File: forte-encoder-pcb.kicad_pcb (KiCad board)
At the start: 6 copper layers, 36.5 x 45 mm, 54 parts, among them J1 Conn_01x01_Pin, J10 Conn_01x01_Pin, J2 BM07B-GHS-TBT, J4 Conn_01x01_Pin, J7 Conn_01x01_Pin, J8 Conn_01x01_Pin, J9 Conn_01x01_Pin, U2 STM32F103C8Tx, U3 MCP2542FD-E/MF, U4 MA732GQ-Z, U5 TPS629203DRLR, U6 TPS629203DRLR, Y1 CSTNE8M00G550000R0

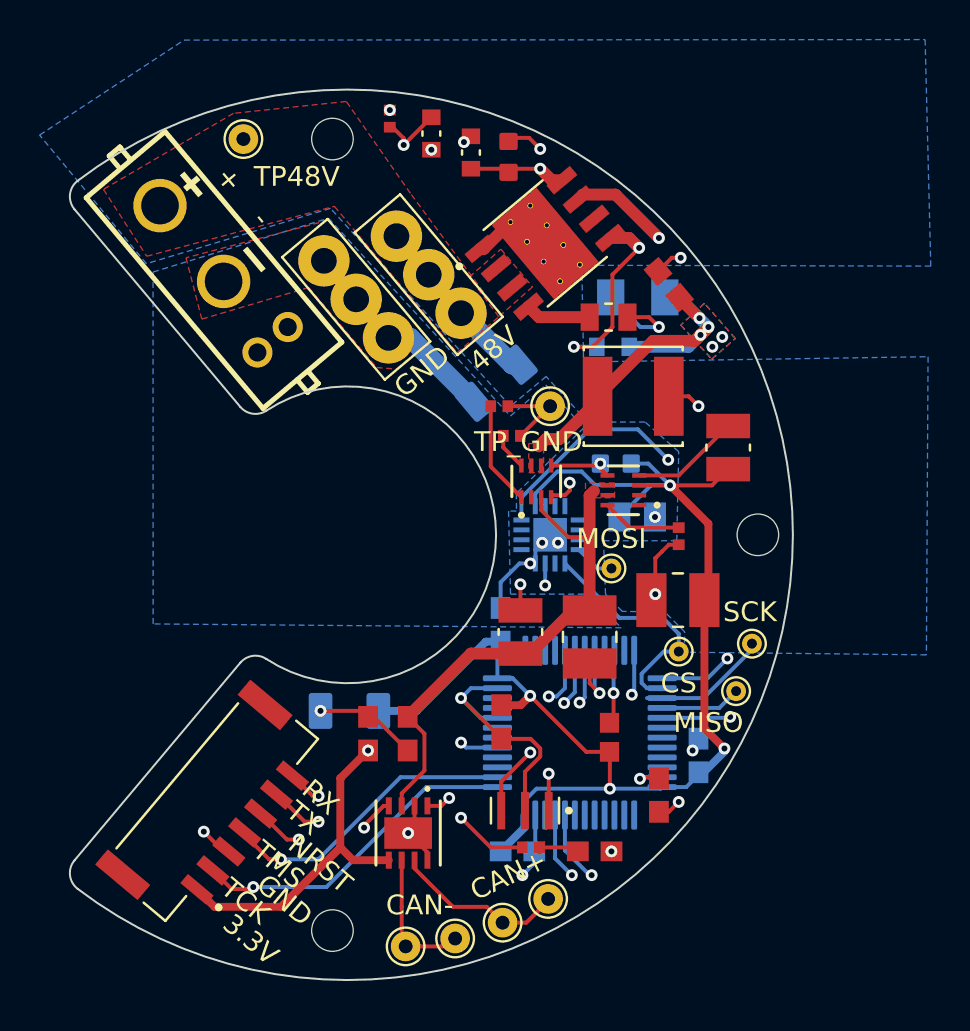
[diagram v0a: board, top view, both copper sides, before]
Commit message: fix TMS PA15->PA13
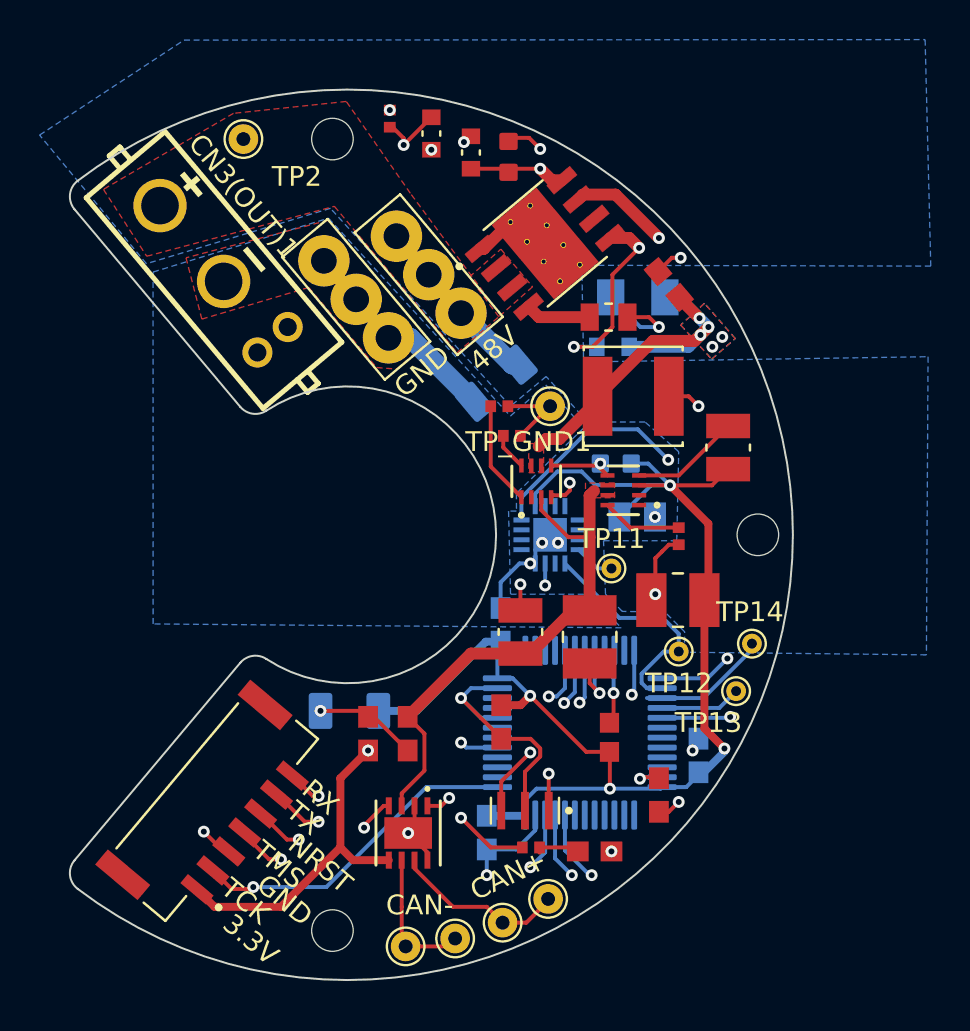
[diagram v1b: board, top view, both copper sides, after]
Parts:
- CN3(OUT)1: renamed from +    -
- moved C29 1.82 mm to (102.8, 115.0), turned to 90 degrees
- renumbered MOSI to TP11, CS to TP12, MISO to TP13, SCK to TP14, TP48V to TP2, TP_GND to TP_GND1
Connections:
- U2 pad 34: unconnected-(U2-PA13-Pad34) -> /TMS
- U2 pad 38: /TMS -> unconnected-(U2-PA15-Pad38)
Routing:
- net /TMS: track 15.1 -> 18.2 mm, vias 1 -> 2
- net GND: track 62.7 -> 64.7 mm
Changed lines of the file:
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@@
 		(layer "F.Cu")
 		(at 89.130397 86.75304 -50)
-		(property "Reference" "+    -"
+		(property "Reference" "CN3(OUT)1"
 			(at -2.071236 -3.525863 130)
 			(layer "F.SilkS")
@@
 		(descr "THT pad as test Point, diameter 1.0mm, hole diameter 0.5mm")
 		(tags "test point THT pad")
-		(property "Reference" "MOSI"
+		(property "Reference" "TP11"
 			(at 0 1.5 0)
 			(layer "F.SilkS")
@@
 		(descr "THT pad as test Point, diameter 1.0mm, hole diameter 0.5mm")
 		(tags "test point THT pad")
-		(property "Reference" "MISO"
+		(property "Reference" "TP13"
 			(at 1.4 -1.6 0)
 			(layer "F.SilkS")
@@
 		(descr "THT pad as test Point, diameter 1.0mm, hole diameter 0.5mm")
 		(tags "test point THT pad")
-		(property "Reference" "SCK"
+		(property "Reference" "TP14"
 			(at 0.1 1.6 0)
 			(layer "F.SilkS")
@@
 		(descr "THT pad as test Point, diameter 1.5mm, hole diameter 0.7mm")
 		(tags "test point THT pad")
-		(property "Reference" "TP_GND"
+		(property "Reference" "TP_GND1"
 			(at 1.1 -1.8 0)
 			(layer "F.SilkS")
@@
 		(descr "THT pad as test Point, diameter 1.5mm, hole diameter 0.7mm")
 		(tags "test point THT pad")
-		(property "Reference" "TP48V"
+		(property "Reference" "TP2"
 			(at 2.7 1.9 0)
 			(layer "F.SilkS")
@@
 		(descr "THT pad as test Point, diameter 1.0mm, hole diameter 0.5mm")
 		(tags "test point THT pad")
-		(property "Reference" "CS"
+		(property "Reference" "TP12"
 			(at 0 -1.6 0)
 			(layer "F.SilkS")
@@
 			(layers "B.Cu" "B.Mask" "B.Paste")
 			(roundrect_rratio 0.25)
-			(net "unconnected-(U2-PA13-Pad34)")
+			(net "/TMS")
 			(pinfunction "PA13_34")
-			(pintype "bidirectional+no_connect")
+			(pintype "bidirectional")
 		)
 		(pad "35" smd roundrect
@@
 			(layers "B.Cu" "B.Mask" "B.Paste")
 			(roundrect_rratio 0.25)
-			(net "/TMS")
+			(net "unconnected-(U2-PA15-Pad38)")
 			(pinfunction "PA15_38")
-			(pintype "bidirectional")
+			(pintype "bidirectional+no_connect")
 		)
 		(pad "39" smd roundrect
@@
 	(footprint "dash:CC0603JRX7R9BB104"
 		(layer "B.Cu")
-		(at 104.35 116 180)
+		(at 102.8 115.05 90)
 		(descr "<b>CAPACITOR</b>")
 		(property "Reference" "C29"
-			(at -0.235808 1.239253 0)
+			(at -0.235808 1.239253 90)
 			(layer "B.SilkS")
 			(hide yes)
@@
 		)
 		(property "Value" "100nF 50V"
-			(at 1.567319 -1.206787 0)
+			(at 1.567319 -1.206787 90)
 			(layer "B.Fab")
 			(effects
@@
 		)
 		(property "Datasheet" ""
-			(at 0 0 0)
+			(at 0 0 90)
 			(layer "B.Fab")
 			(hide yes)
@@
 		)
 		(property "Description" ""
-			(at 0 0 0)
+			(at 0 0 90)
 			(layer "B.Fab")
 			(hide yes)
@@
 		(duplicate_pad_numbers_are_jumpers no)
 		(fp_line
-			(start 1.673 0.783)
-			(end 1.673 -0.783)
+			(start 1.673 -0.783)
+			(end -1.673 -0.783)
 			(stroke
 				(width 0.0508)
@@
 		)
 		(fp_line
-			(start 1.673 -0.783)
-			(end -1.673 -0.783)
+			(start -1.673 -0.783)
+			(end -1.673 0.783)
 			(stroke
 				(width 0.0508)
@@
 		)
 		(fp_line
-			(start -1.673 0.783)
-			(end 1.673 0.783)
+			(start 1.673 0.783)
+			(end 1.673 -0.783)
 			(stroke
 				(width 0.0508)
@@
 		)
 		(fp_line
-			(start -1.673 -0.783)
-			(end -1.673 0.783)
+			(start -1.673 0.783)
+			(end 1.673 0.783)
 			(stroke
 				(width 0.0508)
@@
 		)
 		(fp_line
-			(start -0.356 0.432)
-			(end 0.356 0.432)
+			(start -0.356 -0.419)
+			(end 0.356 -0.419)
 			(stroke
 				(width 0.1016)
@@
 		)
 		(fp_line
-			(start -0.356 -0.419)
-			(end 0.356 -0.419)
+			(start -0.356 0.432)
+			(end 0.356 0.432)
 			(stroke
 				(width 0.1016)
@@
 		)
 		(pad "1" smd rect
-			(at -0.85 0 180)
+			(at -0.85 0 90)
 			(size 1.1 1)
 			(layers "B.Cu" "B.Mask" "B.Paste")
@@
 		)
 		(pad "2" smd rect
-			(at 0.85 0 180)
+			(at 0.85 0 90)
 			(size 1.1 1)
 			(layers "B.Cu" "B.Mask" "B.Paste")
@@
 	)
 	(segment
-		(start 103.5 116)
-		(end 104.7 114.8)
+		(start 104.6625 114.2)
+		(end 104.7 114.1625)
 		(width 0.4)
 		(layer "B.Cu")
@@
 	)
 	(segment
-		(start 105.314449 112.828141)
-		(end 109.02 112.828141)
-		(width 0.2)
+		(start 102.8 114.2)
+		(end 104.6625 114.2)
+		(width 0.4)
 		(layer "B.Cu")
 		(net "+3.3V")
 	)
 	(segment
-		(start 104.7 114.8)
-		(end 104.7 114.1625)
-		(width 0.4)
+		(start 105.314449 112.828141)
+		(end 109.02 112.828141)
+		(width 0.2)
 		(layer "B.Cu")
 		(net "+3.3V")
@@
 	)
 	(via
-		(at 104.6 117.2)
+		(at 102.8 117.2)
 		(size 0.6)
 		(drill 0.3)
@@
 	)
 	(segment
+		(start 102.8 115.9)
+		(end 102.8 117.2)
+		(width 0.2)
+		(layer "B.Cu")
+		(net "GND")
+	)
+	(segment
 		(start 109.062 88)
 		(end 110.562 89.5)
@@
 	)
 	(segment
+		(start 102.8 115.9)
+		(end 104.28241 115.9)
+		(width 0.2)
+		(layer "B.Cu")
+		(net "GND")
+	)
+	(segment
+		(start 105.25 114.93241)
+		(end 105.25 114.1625)
+		(width 0.2)
+		(layer "B.Cu")
+		(net "GND")
+	)
+	(segment
 		(start 101.5 108.25)
 		(end 102.5 109.25)
@@
 	)
 	(segment
-		(start 105.2 116.6)
-		(end 104.6 117.2)
-		(width 0.2)
-		(layer "B.Cu")
-		(net "GND")
-	)
-	(segment
 		(start 104.4522 101.4478)
 		(end 105 101.4478)
@@
 	)
 	(segment
-		(start 105.2 116)
-		(end 105.2 116.6)
-		(width 0.2)
-		(layer "B.Cu")
-		(net "GND")
-	)
-	(segment
 		(start 110.562 89.5)
 		(end 111.5 89.5)
@@
 	)
 	(segment
-		(start 105.25 114.1625)
-		(end 105.25 115.61)
+		(start 105.6 100.4)
+		(end 106 100)
 		(width 0.2)
 		(layer "B.Cu")
@@
 	)
 	(segment
-		(start 105.6 100.4)
-		(end 106 100)
+		(start 104.28241 115.9)
+		(end 105.25 114.93241)
 		(width 0.2)
 		(layer "B.Cu")
@@
 	)
 	(via
+		(at 105 116.8)
+		(size 0.6)
+		(drill 0.3)
+		(layers "F.Cu" "B.Cu")
+		(net "/TMS")
+	)
+	(via
 		(at 92.4 116.4)
 		(size 0.6)
@@
 	)
 	(segment
-		(start 98.442893 112.25)
-		(end 103.3375 112.25)
+		(start 105.75 116.05)
+		(end 105 116.8)
 		(width 0.2)
 		(layer "B.Cu")
@@
 	)
 	(segment
-		(start 94.292893 116.4)
-		(end 98.442893 112.25)
+		(start 105.75 114.1625)
+		(end 105.75 116.05)
 		(width 0.2)
 		(layer "B.Cu")
@@
 	)
 	(segment
+		(start 104.6 116.4)
+		(end 105 116.8)
+		(width 0.2)
+		(layer "In3.Cu")
+		(net "/TMS")
+	)
+	(segment
 		(start 92.4 116.4)
-		(end 94.292893 116.4)
+		(end 104.6 116.4)
 		(width 0.2)
-		(layer "B.Cu")
+		(layer "In3.Cu")
 		(net "/TMS")
 	)

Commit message: swap can
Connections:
- CN3(OUT)1 pad 1: /CAN+ -> /CAN-
- CN3(OUT)1 pad 2: /CAN- -> /CAN+
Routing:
- net /CAN+: track 49.8 -> 50.7 mm
- net /CAN-: track 49.4 -> 48.6 mm
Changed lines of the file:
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@@
 			(layers "*.Cu" "*.Mask")
 			(remove_unused_layers no)
-			(net "/CAN+")
+			(net "/CAN-")
 			(pintype "unspecified")
 			(thermal_bridge_angle 90)
@@
 			(layers "*.Cu" "*.Mask")
 			(remove_unused_layers no)
-			(net "/CAN-")
+			(net "/CAN+")
 			(pintype "unspecified")
 			(thermal_bridge_angle 90)
@@
 	)
 	(segment
-		(start 92.323112 91.9)
-		(end 91.208687 90.785575)
+		(start 98.7 120.8)
+		(end 97.95 120.05)
 		(width 0.2)
 		(layer "In1.Cu")
@@
 	)
 	(segment
-		(start 98.7 120.8)
-		(end 97.95 120.05)
+		(start 97.8 91.9)
+		(end 95.140776 91.9)
 		(width 0.2)
 		(layer "In1.Cu")
@@
 	)
 	(segment
-		(start 99 108)
-		(end 104 103)
+		(start 100.045753 92.545753)
+		(end 98.445753 92.545753)
 		(width 0.2)
 		(layer "In1.Cu")
@@
 	)
 	(segment
-		(start 104 96.5)
-		(end 100.045753 92.545753)
+		(start 97.95 120.05)
+		(end 97.95 109.05)
 		(width 0.2)
 		(layer "In1.Cu")
@@
 	)
 	(segment
-		(start 98.445753 92.545753)
-		(end 97.8 91.9)
+		(start 104 96.5)
+		(end 100.045753 92.545753)
 		(width 0.2)
 		(layer "In1.Cu")
@@
 	)
 	(segment
-		(start 100.045753 92.545753)
-		(end 98.445753 92.545753)
+		(start 97.95 109.05)
+		(end 104 103)
 		(width 0.2)
 		(layer "In1.Cu")
@@
 	)
 	(segment
-		(start 97.95 109.05)
-		(end 99 108)
+		(start 95.140776 91.9)
+		(end 92.740776 89.5)
 		(width 0.2)
 		(layer "In1.Cu")
@@
 	)
 	(segment
-		(start 97.8 91.9)
-		(end 92.323112 91.9)
+		(start 98.445753 92.545753)
+		(end 97.8 91.9)
 		(width 0.2)
 		(layer "In1.Cu")
@@
 	)
 	(segment
-		(start 97.95 120.05)
-		(end 97.95 109.05)
+		(start 92.740776 89.740776)
+		(end 92.740776 89.5)
 		(width 0.2)
-		(layer "In1.Cu")
+		(layer "In2.Cu")
 		(net "/CAN-")
 	)
@@
 	)
 	(segment
-		(start 92.740776 89.740776)
-		(end 92.740776 89.5)
-		(width 0.2)
-		(layer "In2.Cu")
-		(net "/CAN+")
-	)
-	(segment
-		(start 99.5 115.5)
-		(end 99.5 108)
+		(start 103.6 119.6)
+		(end 99.5 115.5)
 		(width 0.2)
 		(layer "In2.Cu")
@@
 	)
 	(segment
-		(start 99.5 108)
-		(end 104 103.5)
+		(start 104 96.5)
+		(end 99.5 92)
 		(width 0.2)
 		(layer "In2.Cu")
@@
 	)
 	(segment
-		(start 95 92)
-		(end 92.740776 89.740776)
+		(start 99.5 115.5)
+		(end 99.5 108)
 		(width 0.2)
 		(layer "In2.Cu")
@@
 	)
 	(segment
-		(start 104 96.5)
-		(end 99.5 92)
+		(start 92.423112 92)
+		(end 91.208687 90.785575)
 		(width 0.2)
 		(layer "In2.Cu")
@@
 	)
 	(segment
-		(start 99.5 92)
-		(end 95 92)
+		(start 99.5 108)
+		(end 104 103.5)
 		(width 0.2)
 		(layer "In2.Cu")
@@
 	)
 	(segment
-		(start 103.6 119.6)
-		(end 99.5 115.5)
+		(start 99.5 92)
+		(end 92.423112 92)
 		(width 0.2)
 		(layer "In2.Cu")

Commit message: some shifts
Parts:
- moved TP2 4.90 mm to (95.4, 79.8)
- moved H1 3.41 mm to (91.6, 80.3)
- moved H3 3.41 mm to (91.6, 119.7)
- moved J8 3.02 mm to (96.2, 119.1)
- moved C31 2.78 mm to (106.2, 103.7), turned to 180 degrees
- moved J9 2.64 mm to (98.9, 119.1)
- moved C32 2.54 mm to (95.4, 111.4)
- moved J10 2.21 mm to (101.5, 118.9)
- moved J7 1.81 mm to (104.1, 118.2)
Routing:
- net +3.3V: track 96.5 -> 101.8 mm
- net /CAN+: track 50.7 -> 46.9 mm
- net /CAN-: track 48.6 -> 45.4 mm
- net GND: track 64.7 -> 67.3 mm

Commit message: more fix
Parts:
- removed TP_GND1: GND TestPoint, TestPoint:TestPoint_THTPad_D1.5mm_Drill0.7mm
- moved C37 1.92 mm to (105.0, 93.2), turned to 130 degrees
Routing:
- net GND: track 67.3 -> 61.6 mm, vias 17 -> 18
- net +48V: track 5.34 -> 1.36 mm
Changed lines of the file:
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@@
 		)
 	)
-	(footprint "TestPoint:TestPoint_THTPad_D1.5mm_Drill0.7mm"
-		(layer "F.Cu")
-		(at 106 93.5 180)
-		(descr "THT pad as test Point, diameter 1.5mm, hole diameter 0.7mm")
-		(tags "test point THT pad")
-		(property "Reference" "TP_GND1"
-			(at 1.1 -1.8 0)
-			(layer "F.SilkS")
-			(effects
-				(font
-					(size 1 1)
-					(thickness 0.15)
-				)
-			)
-		)
-		(property "Value" "GND TestPoint"
-			(at 0 1.75 0)
-			(layer "F.Fab")
-			(effects
-				(font
-					(size 1 1)
-					(thickness 0.15)
-				)
-			)
-		)
-		(property "Datasheet" ""
-			(at 0 0 180)
-			(unlocked yes)
-			(layer "F.Fab")
-			(hide yes)
-			(effects
-				(font
-					(size 1.27 1.27)
-					(thickness 0.15)
-				)
-			)
-		)
-		(property "Description" "test point"
-			(at 0 0 180)
-			(unlocked yes)
-			(layer "F.Fab")
-			(hide yes)
-			(effects
-				(font
-					(size 1.27 1.27)
-					(thickness 0.15)
-				)
-			)
-		)
-		(property ki_fp_filters "Pin* Test*")
-		(sheetname "/")
-		(sheetfile "forte-encoder-pcb.kicad_sch")
-		(units
-			(unit
-				(name "A")
-				(pins "1")
-			)
-		)
-		(duplicate_pad_numbers_are_jumpers no)
-		(fp_circle
-			(center 0 0)
-			(end 0 0.95)
-			(stroke
-				(width 0.12)
-				(type solid)
-			)
-			(fill no)
-			(layer "F.SilkS")
-		)
-		(fp_circle
-			(center 0 0)
-			(end 1.25 0)
-			(stroke
-				(width 0.05)
-				(type solid)
-			)
-			(fill no)
-			(layer "F.CrtYd")
-		)
-		(fp_text user "${REFERENCE}"
-			(at 0 -1.65 0)
-			(layer "F.Fab")
-			(effects
-				(font
-					(size 1 1)
-					(thickness 0.15)
-				)
-			)
-		)
-		(pad "1" thru_hole circle
-			(at 0 0 180)
-			(size 1.5 1.5)
-			(drill 0.7)
-			(layers "*.Cu" "*.Mask")
-			(remove_unused_layers no)
-			(net "GND")
-			(pinfunction "1_1")
-			(pintype "passive")
-		)
-		(embedded_fonts no)
-	)
 	(footprint "dash:RT0603BRD07448KL"
 		(layer "F.Cu")
@@
 	(footprint "dash:CL31B225KCHSNNE"
 		(layer "B.Cu")
-		(at 103.281575 92.33847 40)
+		(at 105 93.2 130)
 		(property "Reference" "C37"
-			(at -1.06 1.499999 40)
+			(at -1.06 1.499999 130)
 			(layer "B.SilkS")
 			(hide yes)
@@
 		)
 		(property "Value" "CL31B225KCHSNNE"
-			(at 0.94 -1.5 40)
+			(at 0.94 -1.5 130)
 			(layer "B.Fab")
 			(effects
@@
 		)
 		(property "Datasheet" ""
-			(at 0 0 40)
+			(at 0 0 130)
 			(layer "B.Fab")
 			(hide yes)
@@
 		)
 		(property "Description" "2.2uF"
-			(at 0 0 40)
+			(at 0 0 130)
 			(layer "B.Fab")
 			(hide yes)
@@
 		)
 		(property "E_max" "1.8"
-			(at 0 0 220)
+			(at 0 0 310)
 			(unlocked yes)
 			(layer "B.Fab")
@@
 		)
 		(property "L_max" "0.8"
-			(at 0 0 220)
+			(at 0 0 310)
 			(unlocked yes)
 			(layer "B.Fab")
@@
 		)
 		(property "A_max" "1.8"
-			(at 0 0 220)
+			(at 0 0 310)
 			(unlocked yes)
 			(layer "B.Fab")
@@
 		)
 		(property "L1_nom" "0.5"
-			(at 0 0 220)
+			(at 0 0 310)
 			(unlocked yes)
 			(layer "B.Fab")
@@
 		)
 		(property "D_max" "3.4"
-			(at 0 0 220)
+			(at 0 0 310)
 			(unlocked yes)
 			(layer "B.Fab")
@@
 		)
 		(property "A_nom" "1.8"
-			(at 0 0 220)
+			(at 0 0 310)
 			(unlocked yes)
 			(layer "B.Fab")
@@
 		)
 		(property "L1_max" "0.8"
-			(at 0 0 220)
+			(at 0 0 310)
 			(unlocked yes)
 			(layer "B.Fab")
@@
 		)
 		(property "L1_min" "0.2"
-			(at 0 0 220)
+			(at 0 0 310)
 			(unlocked yes)
 			(layer "B.Fab")
@@
 		)
 		(property "A_min" "1.8"
-			(at 0 0 220)
+			(at 0 0 310)
 			(unlocked yes)
 			(layer "B.Fab")
@@
 		)
 		(property "E_min" "1.4"
-			(at 0 0 220)
+			(at 0 0 310)
 			(unlocked yes)
 			(layer "B.Fab")
@@
 		)
 		(property "D_min" "3.0"
-			(at 0 0 220)
+			(at 0 0 310)
 			(unlocked yes)
 			(layer "B.Fab")
@@
 		)
 		(property "D_nom" "3.2"
-			(at 0 0 220)
+			(at 0 0 310)
 			(unlocked yes)
 			(layer "B.Fab")
@@
 		)
 		(property "E_nom" "1.6"
-			(at 0 0 220)
+			(at 0 0 310)
 			(unlocked yes)
 			(layer "B.Fab")
@@
 		)
 		(property "STANDARD" "IPC 7351B"
-			(at 0 0 220)
+			(at 0 0 310)
 			(unlocked yes)
 			(layer "B.Fab")
@@
 		)
 		(property "L_min" "0.2"
-			(at 0 0 220)
+			(at 0 0 310)
 			(unlocked yes)
 			(layer "B.Fab")
@@
 		)
 		(property "L_nom" "0.5"
-			(at 0 0 220)
+			(at 0 0 310)
 			(unlocked yes)
 			(layer "B.Fab")
@@
 		)
 		(property "MANUFACTURER" "Samsung Electro-Mechanics"
-			(at 0 0 220)
+			(at 0 0 310)
 			(unlocked yes)
 			(layer "B.Fab")
@@
 		)
 		(fp_line
-			(start -2.310001 -1.16)
-			(end -2.31 1.16)
+			(start 2.31 -1.16)
+			(end 2.310001 1.16)
 			(stroke
 				(width 0.05)
@@
 		)
 		(fp_line
-			(start -2.31 1.16)
-			(end 2.310001 1.16)
+			(start -2.310001 -1.16)
+			(end -2.31 1.16)
 			(stroke
 				(width 0.05)
@@
 		)
 		(fp_line
-			(start 2.31 -1.16)
+			(start -2.31 1.16)
 			(end 2.310001 1.16)
 			(stroke
@@
 		)
 		(fp_line
-			(start -1.6 -0.8)
-			(end -1.6 0.799999)
+			(start 1.6 -0.799999)
+			(end 1.6 0.8)
 			(stroke
 				(width 0.127)
@@
 		)
 		(fp_line
-			(start 1.6 -0.799999)
-			(end 1.6 0.8)
+			(start 1.6 0.8)
+			(end -1.6 0.799999)
 			(stroke
 				(width 0.127)
@@
 		)
 		(fp_line
-			(start 1.6 0.8)
+			(start -1.6 -0.8)
 			(end -1.6 0.799999)
 			(stroke
@@
 		)
 		(pad "1" smd roundrect
-			(at -1.46 0 40)
+			(at -1.46 0 130)
 			(size 1.2 1.82)
 			(layers "B.Cu" "B.Mask" "B.Paste")
@@
 		)
 		(pad "2" smd roundrect
-			(at 1.46 0 40)
+			(at 1.46 0 130)
 			(size 1.2 1.82)
 			(layers "B.Cu" "B.Mask" "B.Paste")
@@
 	)
 	(via
+		(at 106 93.5)
+		(size 0.6)
+		(drill 0.3)
+		(layers "F.Cu" "B.Cu")
+		(net "GND")
+	)
+	(via
 		(at 105.6 100.4)
 		(size 0.6)
@@
 	)
 	(segment
-		(start 98.931963 90.045753)
-		(end 102.16315 93.27694)
-		(width 1)
-		(layer "B.Cu")
-		(net "GND")
-	)
-	(segment
 		(start 108.631 87.5)
 		(end 108.631 88.631)
@@
 	)
 	(segment
-		(start 97.832681 90.045753)
-		(end 98.931963 90.045753)
-		(width 1)
-		(layer "B.Cu")
-		(net "GND")
-	)
-	(segment
 		(start 102 107.75)
 		(end 103.3375 107.75)
@@
 		(net "+48V")
 	)
-	(segment
-		(start 104.4 91.4)
-		(end 104.1 91.4)
-		(width 1)
-		(layer "B.Cu")
-		(net "+48V")
-	)
-	(segment
-		(start 104.1 91.4)
-		(end 101.5 88.8)
-		(width 1)
-		(layer "B.Cu")
-		(net "+48V")
-	)
